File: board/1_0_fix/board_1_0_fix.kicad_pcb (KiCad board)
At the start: 2 copper layers, 19 x 18 mm, 11 parts

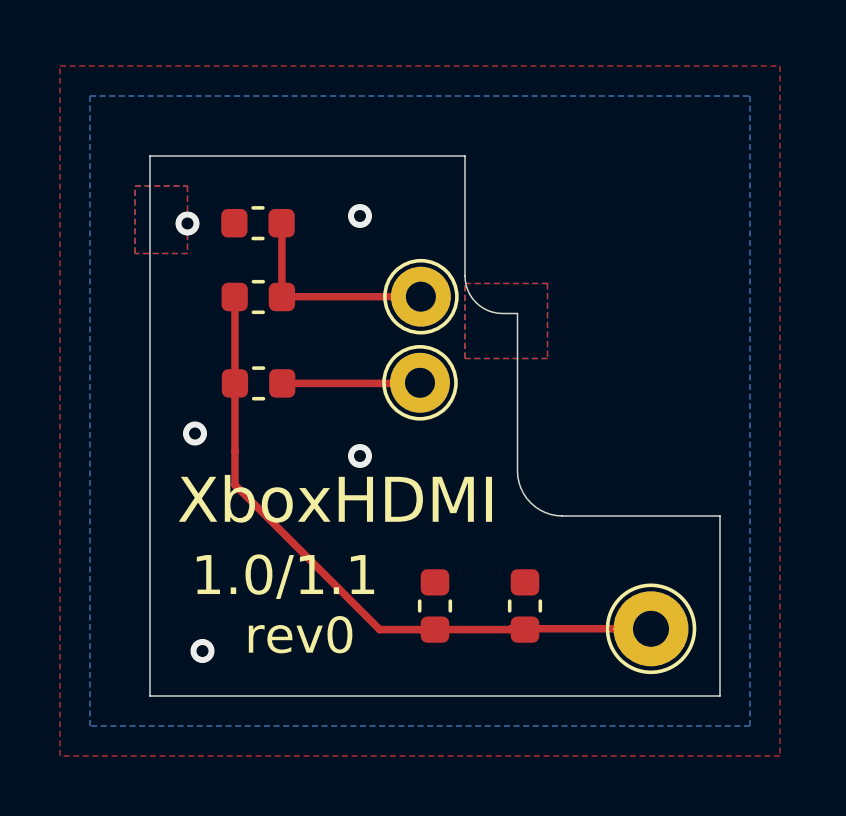
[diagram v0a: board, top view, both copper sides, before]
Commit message: Fix board layout for production
Small adjustments to layout for the production run of rev0
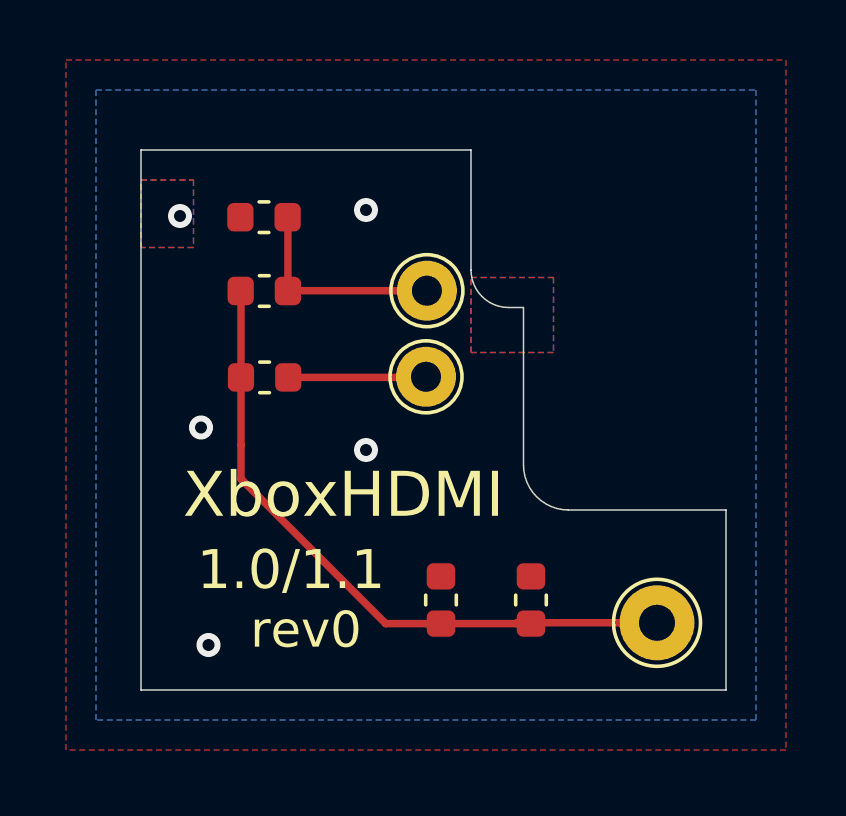
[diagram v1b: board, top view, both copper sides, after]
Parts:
- moved C2 0.28 mm to (33.7, 37.8)
- moved C1 0.28 mm to (30.7, 37.8)
- moved LOGO1 0.28 mm to (31.7, 37.0)
- moved LOGO2 0.28 mm to (25.2, 32.3)
- moved TP3 0.28 mm to (30.2, 27.5)
- moved R4B7 0.28 mm to (24.8, 30.4)
- moved R4M7 0.28 mm to (24.8, 27.5)
- moved R4N14 0.28 mm to (24.8, 25.0)
- moved TP2 0.28 mm to (30.2, 30.4)
- moved TP1 0.28 mm to (37.9, 38.6)
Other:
- board size 19 x 18 mm -> 19.5 x 18 mm
